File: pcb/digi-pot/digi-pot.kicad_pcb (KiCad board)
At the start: 2 copper layers, 25 x 31 mm, 14 parts, among them IC1 ATTINY48-M, P1 CONN_01X04, P2 CONN_01X05, P3 CONN_01X12, P4 CONN_01X03, P5 CONN_01X03, U1 CUI-C14, U2 DS1882

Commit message: o Better marking of input voltages.
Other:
- board text added: "Analog+"
- board text added: "Analog-"
- board text added: "Hi"
- board text added: "Lo"
- board text removed: "High"
- board text removed: "Low"
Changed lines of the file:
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@@
-(kicad_pcb (version 20160815) (host pcbnew "(2016-10-23 revision 4ee344e)-master")
+(kicad_pcb (version 20160815) (host pcbnew "(2016-10-07 revision f14dc8f)-master")
   (general
     (links 60)
     (no_connects 0)
-    (area 99.031667 59.9825 142.000001 99.745)
+    (area 101.924999 62.924999 127.075001 94.075001)
     (thickness 1.6)
-    (drawings 42)
+    (drawings 45)
     (tracks 286)
     (zones 0)
@@
     )
   )
+  (gr_text Analog- (at 118.11 67.945 90) (layer B.SilkS)
+    (effects (font (size 1.2 1.2) (thickness 0.25)) (justify left mirror))
+  )
+  (gr_text GND (at 115.57 67.945 90) (layer B.SilkS)
+    (effects (font (size 1.2 1.2) (thickness 0.25)) (justify left mirror))
+  )
+  (gr_text Analog+ (at 113.03 67.945 90) (layer B.SilkS)
+    (effects (font (size 1.2 1.2) (thickness 0.25)) (justify left mirror))
+  )
   (gr_text %%gitversion%% (at 104.1 73.1 90) (layer B.SilkS)
     (effects (font (size 1.1 1.1) (thickness 0.15)) (justify left mirror))
@@
     (effects (font (size 1.5 1.5) (thickness 0.3)) (justify left))
   )
-  (gr_text High (at 104.1 73.6) (layer F.SilkS)
+  (gr_text Hi (at 106.68 72.39 90) (layer F.SilkS)
     (effects (font (size 1 1) (thickness 0.15)))
   )
-  (gr_text High (at 124.5 73.5) (layer F.SilkS)
+  (gr_text Hi (at 121.92 72.39 90) (layer F.SilkS)
     (effects (font (size 1 1) (thickness 0.15)))
   )
-  (gr_text Low (at 124.3 63.7) (layer F.SilkS)
+  (gr_text Lo (at 121.92 64.77 90) (layer F.SilkS)
     (effects (font (size 1 1) (thickness 0.15)))
   )
-  (gr_text Low (at 104.1 63.7) (layer F.SilkS)
+  (gr_text Lo (at 106.68 64.77 90) (layer F.SilkS)
     (effects (font (size 1 1) (thickness 0.15)))
   )
-  (gr_text 5V (at 107.4 64.7) (layer F.SilkS)
-    (effects (font (size 1.5 1.5) (thickness 0.3)))
+  (gr_text 5V (at 110.49 67.945 90) (layer B.SilkS)
+    (effects (font (size 1.2 1.2) (thickness 0.25)) (justify left mirror))
   )
   (gr_text RST (at 124.4 89.8 90) (layer F.SilkS)
-    (effects (font (size 1.5 1.5) (thickness 0.3)))
+    (effects (font (size 1.2 1.2) (thickness 0.25)))
   )
   (gr_text GND (at 120.7 75.5) (layer F.SilkS)
-    (effects (font (size 1.5 1.5) (thickness 0.3)))
+    (effects (font (size 1.2 1.2) (thickness 0.25)))
   )
   (gr_line (start 118.8 69.7) (end 119.3 70.6) (layer F.SilkS) (width 0.2))
@@
     (arrow2b (pts (xy 129 63) (xy 129.586421 64.126504)))
   )
-  (dimension 27 (width 0.3) (layer F.SilkS)
-    (gr_text "27.000 mm" (at 115.5 98.349999) (layer F.SilkS)
+  (dimension 25 (width 0.3) (layer F.SilkS)
+    (gr_text "25.000 mm" (at 114.5 98.35) (layer F.SilkS)
       (effects (font (size 1.5 1.5) (thickness 0.3)))
     )
-    (feature1 (pts (xy 129 96) (xy 129 99.699999)))
-    (feature2 (pts (xy 102 96) (xy 102 99.699999)))
-    (crossbar (pts (xy 102 96.999999) (xy 129 96.999999)))
-    (arrow1a (pts (xy 129 96.999999) (xy 127.873496 97.58642)))
-    (arrow1b (pts (xy 129 96.999999) (xy 127.873496 96.413578)))
-    (arrow2a (pts (xy 102 96.999999) (xy 103.126504 97.58642)))
-    (arrow2b (pts (xy 102 96.999999) (xy 103.126504 96.413578)))
+    (feature1 (pts (xy 127 96) (xy 127 99.7)))
+    (feature2 (pts (xy 102 96) (xy 102 99.7)))
+    (crossbar (pts (xy 102 97) (xy 127 97)))
+    (arrow1a (pts (xy 127 97) (xy 125.873496 97.586421)))
+    (arrow1b (pts (xy 127 97) (xy 125.873496 96.413579)))
+    (arrow2a (pts (xy 102 97) (xy 103.126504 97.586421)))
+    (arrow2b (pts (xy 102 97) (xy 103.126504 96.413579)))
   )
   (gr_line (start 102 94) (end 102 63) (layer Edge.Cuts) (width 0.15))

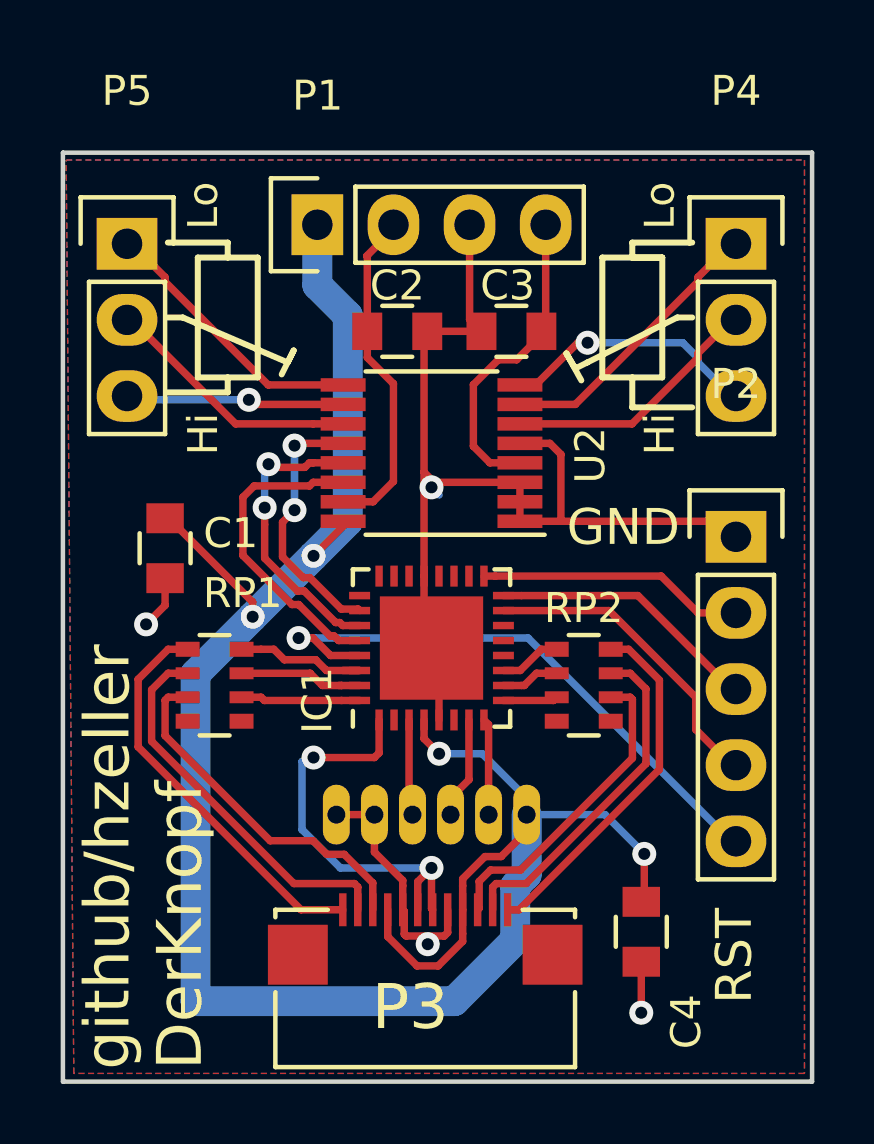
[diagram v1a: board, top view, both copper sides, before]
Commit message: o Add pull-ups for I2C bus. o smallish changes in power supply.
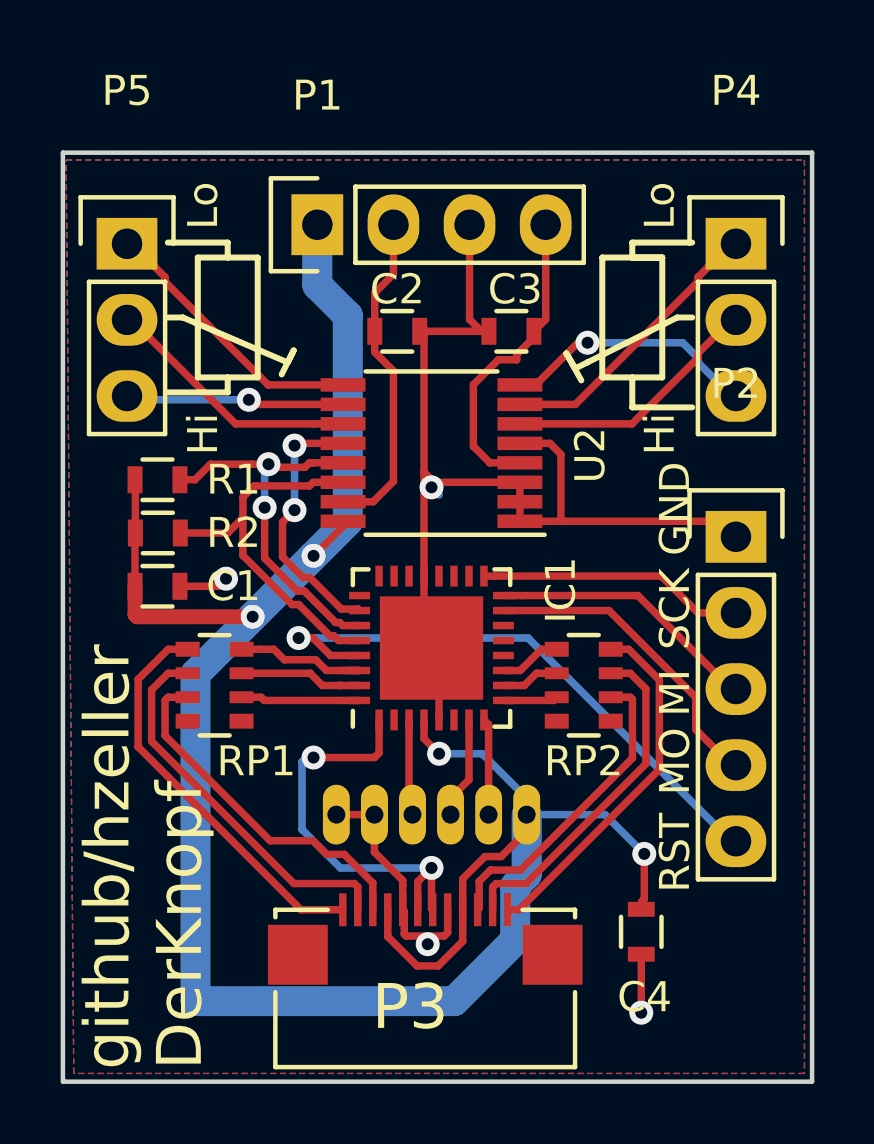
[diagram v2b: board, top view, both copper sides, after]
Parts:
- added R1: 4k7, Resistors_SMD:R_0603, F.Cu at (105.2, 73.9)
- added R2: 4k7, Resistors_SMD:R_0603, F.Cu at (105.2, 75.7)
- C1, C2, C3, C4: footprint Capacitors_SMD:C_0805 -> Resistors_SMD:R_0603
- moved C1 1.30 mm to (105.2, 77.5), turned to 0 degrees
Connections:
- IC1 pad 12: (no net) -> Net-(IC1-Pad12)
- IC1 pad 13: (no net) -> Net-(IC1-Pad13)
- IC1 pad 14: (no net) -> Net-(IC1-Pad14)
- IC1 pad 18: (no net) -> Net-(IC1-Pad18)
- IC1 pad 19: (no net) -> Net-(IC1-Pad19)
- IC1 pad 2: (no net) -> Net-(IC1-Pad2)
- IC1 pad 20: (no net) -> Net-(IC1-Pad20)
- IC1 pad 22: (no net) -> Net-(IC1-Pad22)
- IC1 pad 23: (no net) -> Net-(IC1-Pad23)
- IC1 pad 24: (no net) -> Net-(IC1-Pad24)
- IC1 pad 25: (no net) -> Net-(IC1-Pad25)
- IC1 pad 6: (no net) -> Net-(IC1-Pad6)
- RP1 pad 4: (no net) -> Net-(RP1-Pad4)
- RP1 pad 5: (no net) -> Net-(RP1-Pad5)
- RP2 pad 1: (no net) -> Net-(RP2-Pad1)
- RP2 pad 8: (no net) -> Net-(RP2-Pad8)
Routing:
- net +5V: track 71.5 -> 75.6 mm
- net /SDA: track 9.89 -> 13.1 mm
- net /SCL: track 10.6 -> 12.9 mm
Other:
- net class little-thicker added: clearance 0.2, trace_width 0.5, via_dia 0.8, via_drill 0.4
- board text added: "MI"
- board text added: "MO"
- board text added: "SCK"

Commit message: o connect flat flex connector ground to ground.
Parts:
- P3: value CONN_01X12 -> CONN_01X13
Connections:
- P3 pad 13: (no net) -> GND
